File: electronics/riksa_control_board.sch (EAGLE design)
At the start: 13 parts, among them U1 ARDUINOR3-BPLACE

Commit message: ELE: new version of control board
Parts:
- removed BTN_REVERSE, BTN_STOP: (no value), adafruit:SWITCH_PUSHBUTTONSOFTTOUCHSMD_SJ
- removed LED_BACKWARD, LED_FORKWARD, LED_STOP: (no value), led:LED
- removed POT_LEFT, POT_RIGHT: (no value), rcl:POTENTIOMETER_PT-10S
- removed U1: ARDUINOR3-BPLACE, adafruit:ARDUINOR3-BPLACE
- added ARDUINO_NANO1: (no value), ArduinoNanoV30:ARDUINO_NANO
- added IM1: DEVKITC, esp32:DEVKITC
- added JP1: CON_ROBOCLAW, pinhead:PINHD-2X4
- added JP10, JP9: CON_MPU-6050, pinhead:PINHD-1X8
- added JP11: REPRO, pinhead:PINHD-2X2
- added JP12: VCC_REF_SEL, pinhead:PINHD-1X3
- added JP13: BLUETOOTH, pinhead:PINHD-1X5/90
- added JP2: POT_RIGHT, pinhead:PINHD-2X3
- added JP3: POT_LEFT, pinhead:PINHD-2X3
- added JP4: LED_STOP, pinhead:PINHD-2X2
- added JP5: LED_BACKWARD, pinhead:PINHD-2X2
- added JP6: LED_FORWARD, pinhead:PINHD-2X2
- added JP7: BTN_REVERSE, pinhead:PINHD-2X2
- added JP8: BTN_STOP, pinhead:PINHD-2X2
- added NC1, NC10, NC11, NC12, NC13, NC14, NC15, NC16, NC17, NC18, NC19, NC2, NC20, NC21, NC22, NC23, NC3, NC4, NC5, NC6, NC7, NC8, NC9: NC, NC:NC
- added R10, R9: x, rcl:R-EU_R0805
- added R6: 220, rcl:R-EU_R0805
- added R7: 2k2, rcl:R-EU_R0805
- added R8: 1k, rcl:R-EU_R0805
- R1, R2, R3, R4, R5: device rcl:R-EU_R0603 -> rcl:R-EU_R0805
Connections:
- removed net +5V: POT_LEFT.1, POT_RIGHT.1
- removed net ROBOCLAW_RX: U1.D0
- removed net ROBOCLAW_TX: U1.D1
- new net 3V3: ARDUINO_NANO1.3V3, IM1.3V3, JP12.1
- new net A0_POT_LEFT: ARDUINO_NANO1.ADC0/A0, IM1.IO26, JP3.3, JP3.4
- new net A1_POT_RIGHT: ARDUINO_NANO1.ADC1/A1, IM1.IO27, JP2.3, JP2.4
- new net AD0: JP10.7, JP9.7, NC1.NC
- new net BT_STATE: ARDUINO_NANO1.D7/AIN1, JP13.5
- new net D10_REPRO: ARDUINO_NANO1.D10/OC1B/!SS, IM1.IO25, R6.1
- new net D11_ROBOCLAW_RX: ARDUINO_NANO1.D11/MOSI, JP1.7, JP1.8
- new net D12_ROBOCLAW_TX: ARDUINO_NANO1.D12/MISO, JP1.5, JP1.6
- new net D3_BTN_STOP: ARDUINO_NANO1.D3/INT1, R1.1
- new net D4_BTN_REVERSE: ARDUINO_NANO1.D4/T0, R2.1
- new net D5_LED_FORWADR: ARDUINO_NANO1.D5/T1, R3.1
- new net D6_LED_BACKWARD: ARDUINO_NANO1.D6/AIN0, R4.1
- new net D9_LED_STOP: ARDUINO_NANO1.D9/OC1A, R5.1
- new net GND: ARDUINO_NANO1.GND@1, ARDUINO_NANO1.GND@2, IM1.GND, JP1.3, JP1.4, JP10.2, JP13.2, JP2.5, JP2.6, JP3.5, JP3.6, JP9.2, R10.2, R7.2
- new net MPU_INT: ARDUINO_NANO1.D2/INT0, JP10.8, JP9.8
- new net MPU_SCL: ARDUINO_NANO1.ADC5/SCL/A5, IM1.IO22, JP10.3, JP9.3
- new net MPU_SDA: ARDUINO_NANO1.ADC4/SDA/A4, IM1.IO21, JP10.4, JP9.4
- new net N$13: IM1.EN, NC11.NC
- new net N$15: IM1.IO12, NC17.NC
- new net N$16: IM1.IO15, NC18.NC
- new net N$17: IM1.IO2, NC19.NC
- new net N$18: IM1.IO0, NC20.NC
- new net N$19: IM1.IO5, NC21.NC
- new net N$20: ARDUINO_NANO1.SCK/D13, NC8.NC
- new net N$21: ARDUINO_NANO1.ADC3/A3, NC12.NC
- new net N$22: ARDUINO_NANO1.ADC6/A6, NC13.NC
- new net N$23: ARDUINO_NANO1.ADC7/A7, NC14.NC
- new net N$24: ARDUINO_NANO1.!RESET@1, NC15.NC
- new net N$25: ARDUINO_NANO1.D8/CLK0, NC16.NC
- new net N$26: ARDUINO_NANO1.!RESET@2, NC22.NC
- new net N$27: ARDUINO_NANO1.VIN, NC23.NC
- new net ROBOCLAW_GND1: JP11.3, JP11.4
- new net RX<-: ARDUINO_NANO1.D0/RX, IM1.RXD0, JP13.3
- new net TX->: ARDUINO_NANO1.D1/TX, IM1.TXD0, R8.2
- new net TX->_: JP13.4, R7.1, R8.1
- new net VCC: JP10.1, JP12.2, JP13.1, JP2.1, JP2.2, JP3.1, JP3.2, JP9.1
- new net VOLTAGE_REF: ARDUINO_NANO1.ADC2/A2, IM1.IO14, R10.1, R9.2
- new net XCL: JP10.6, JP9.6, NC2.NC
- new net XDA: JP10.5, JP9.5, NC3.NC
- net N$1: now also IM1.SD1, NC4.NC; no longer R3.1, U1.D5
- net N$10: now also IM1.SD3, NC9.NC; no longer BTN_STOP.P$1, R1.2
- net N$11: now also JP8.1, JP8.2, R1.2; no longer POT_LEFT.3, U1.A0
- net N$12: now also IM1.SD2, NC10.NC; no longer POT_RIGHT.3, U1.A1
- net N$2: now also JP11.1, JP11.2, R6.2; no longer R4.1, U1.D6
- net N$3: now also JP6.1, JP6.2; no longer LED_FORKWARD.A
- net N$4: now also JP5.1, JP5.2; no longer LED_BACKWARD.A
- net N$5: now also IM1.SD0, NC5.NC; no longer R5.1, U1.D11
- net N$6: now also IM1.CLK, NC6.NC; no longer R1.1, U1.D2
- net N$7: now also JP7.1, JP7.2, R2.2; no longer R2.1, U1.D3
- net N$8: now also JP4.1, JP4.2; no longer LED_STOP.A
- net N$9: now also IM1.CMD, NC7.NC; no longer BTN_REVERSE.P$1, R2.2
- net ROBOCLAW_5V: now also ARDUINO_NANO1.5V, IM1.5V, JP1.1, JP1.2, JP12.3, R9.1; no longer U1.5V
- net ROBOCLAW_GND: now also JP4.3, JP4.4, JP5.3, JP5.4, JP6.3, JP6.4, JP7.3, JP7.4, JP8.3, JP8.4; no longer BTN_REVERSE.P$2, BTN_STOP.P$2, LED_BACKWARD.C, LED_FORKWARD.C, LED_STOP.C, POT_LEFT.2, POT_RIGHT.2, U1.GND1
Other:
- note added: "Info: Arduino Nano: add R7 + R8 (for 5V device) ESP32: R8 = 0 Ohm and without R7"
- moved on the sheet: R1, R2, R3, R4, R5

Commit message: ELE: final version of control board
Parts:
- added JP14: EMPTY, pinhead:PINHD-1X2
- added NC24: NC, NC:NC
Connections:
- net N$11 renamed D3_BTN_STOP_
- net N$2 renamed D10_REPRO_
- net N$3 renamed D5_LED_FORWADR_
- net N$4 renamed D6_LED_BACKWARD_
- net N$7 renamed D4_BTN_REVERSE_
- net N$8 renamed D9_LED_STOP_
- removed net ROBOCLAW_GND: JP4.3, JP4.4, JP5.3, JP5.4, JP6.3, JP6.4, JP7.3, JP7.4, JP8.3, JP8.4
- removed net ROBOCLAW_GND1: JP11.3, JP11.4
- new net IO18: IM1.IO18, JP14.2
- new net IO19: IM1.IO19, JP14.1
- new net N$14: ARDUINO_NANO1.AREF, NC24.NC
- net BT_STATE: now also IM1.SVP
- net D11_ROBOCLAW_RX: now also IM1.IO33
- net D12_ROBOCLAW_TX: now also IM1.IO32
- net D3_BTN_STOP: now also IM1.IO35
- net D4_BTN_REVERSE: now also IM1.IO34
- net D5_LED_FORWADR: now also IM1.IO16
- net D6_LED_BACKWARD: now also IM1.IO17
- net D9_LED_STOP: now also IM1.IO4
- net GND: now also JP11.3, JP11.4, JP4.3, JP4.4, JP5.3, JP5.4, JP6.3, JP6.4, JP7.3, JP7.4, JP8.3, JP8.4
- net MPU_INT: now also IM1.SVN

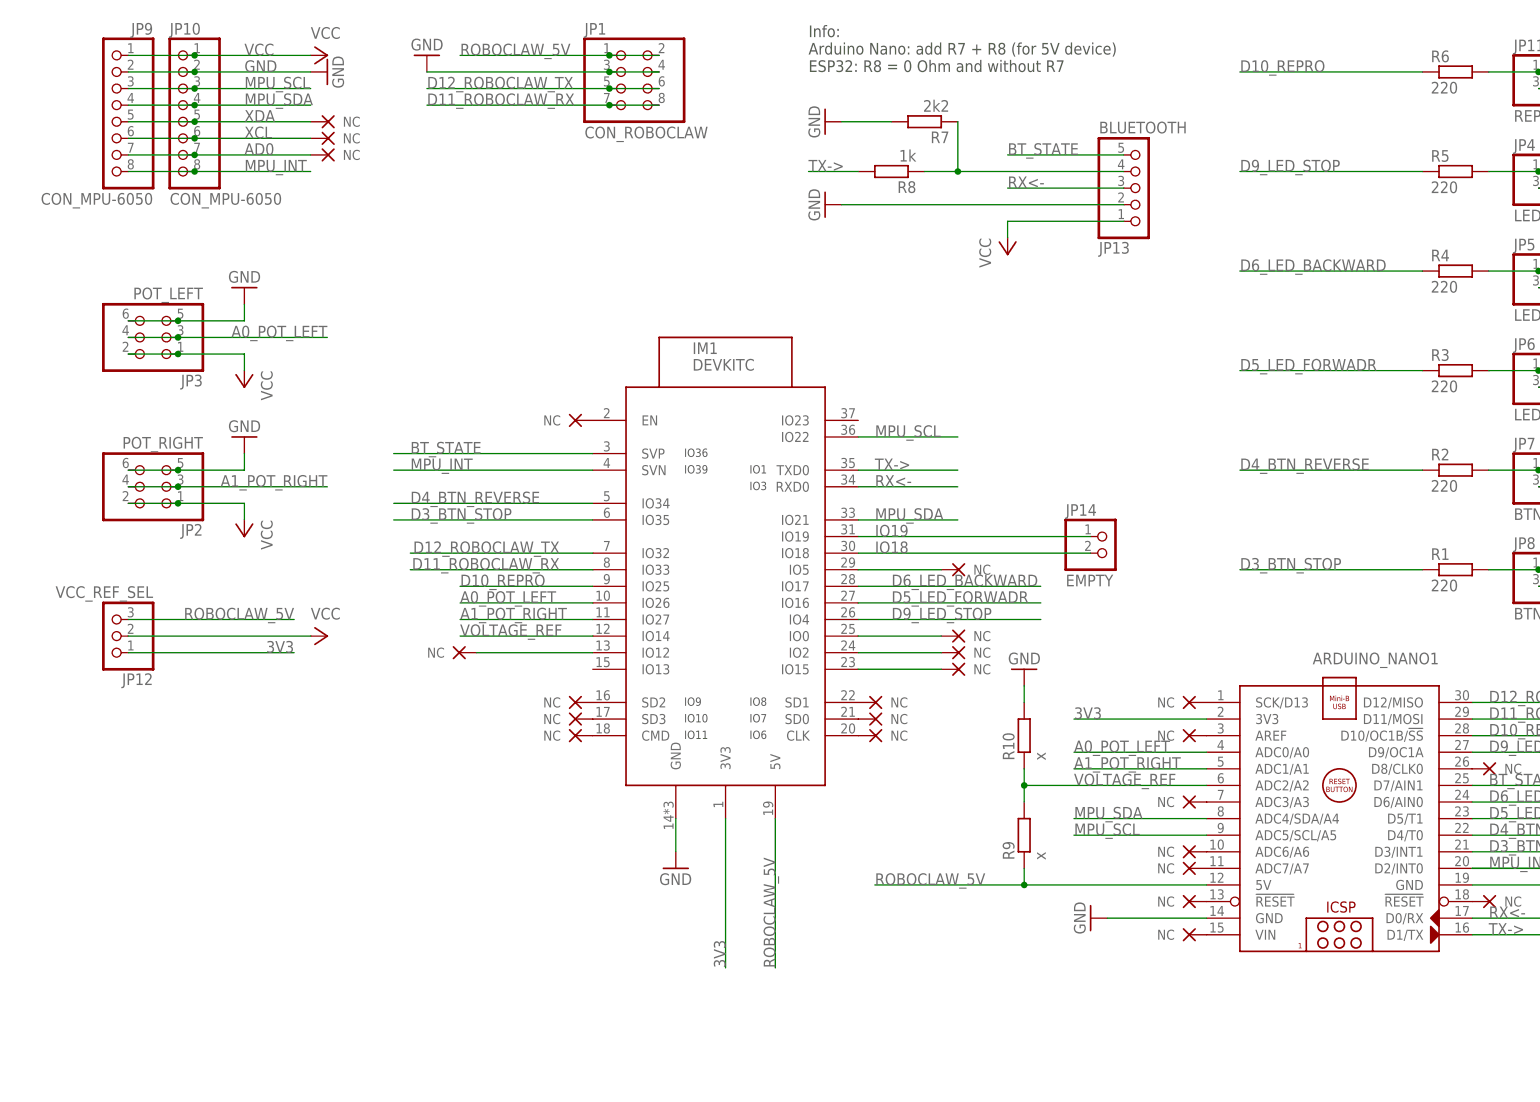
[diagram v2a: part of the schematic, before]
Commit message: ELE: fix Kubas comments
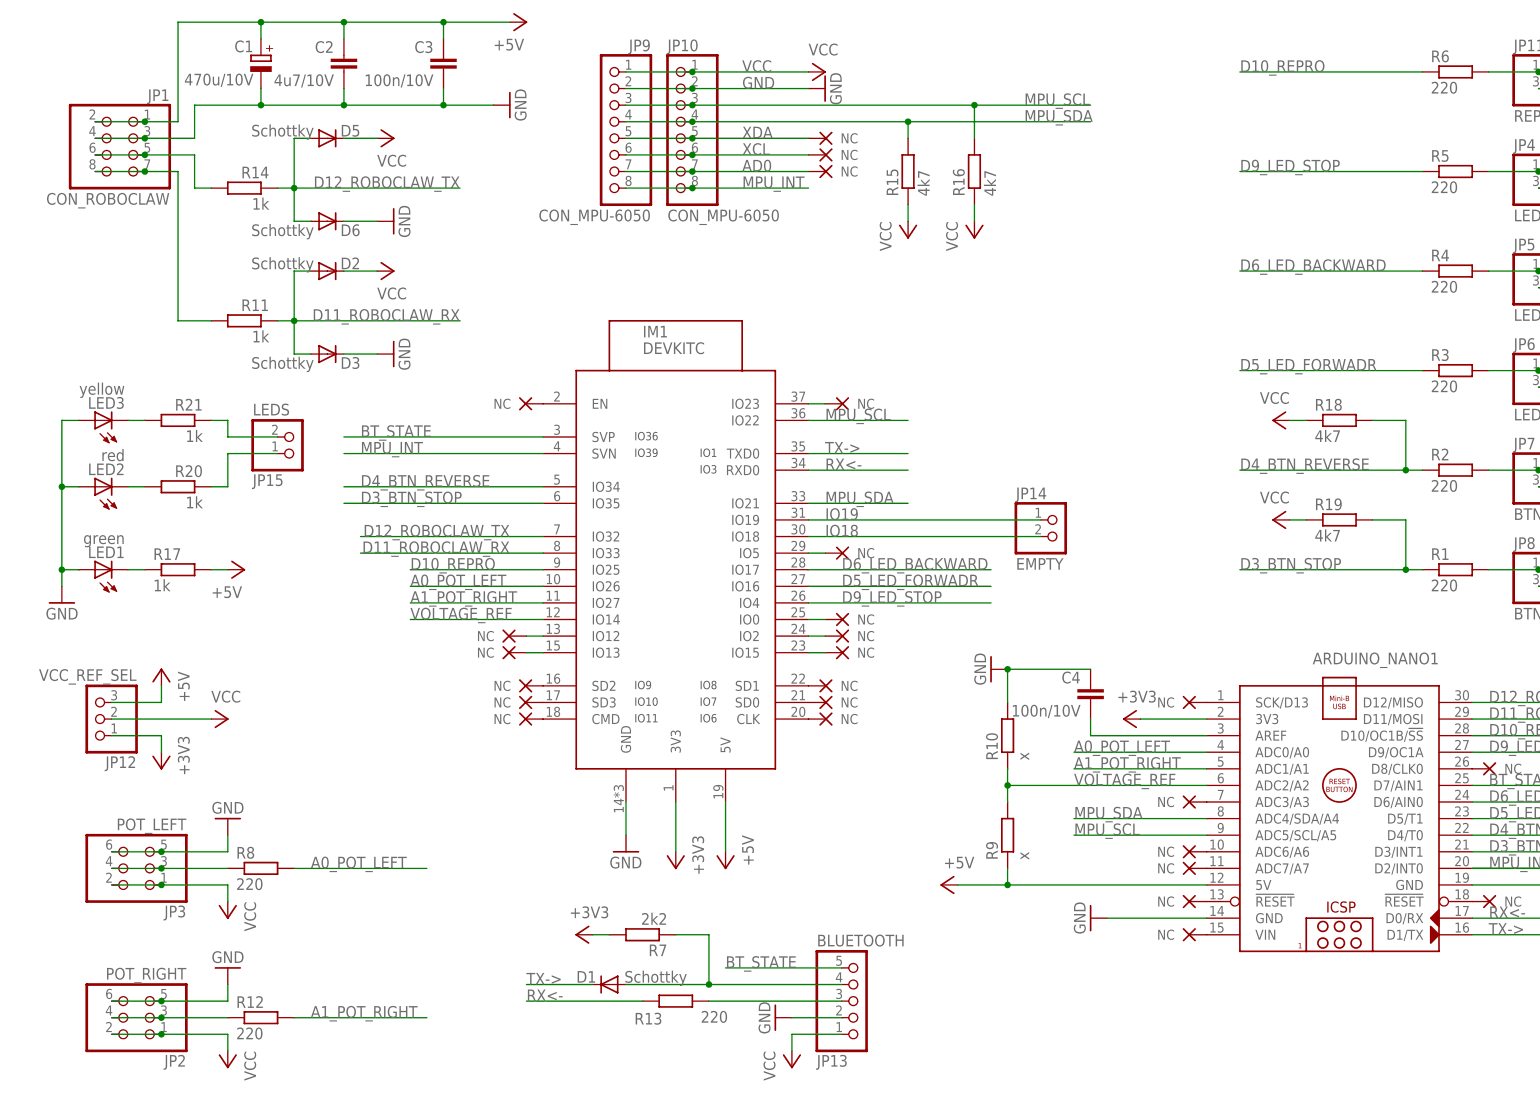
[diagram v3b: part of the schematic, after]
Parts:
- removed NC24: NC, NC:NC
- added C1: 470u/10V, rcl:CPOL-EUTT6D6
- added C2: 4u7/10V, rcl:C-EUC0805
- added C3, C4: 100n/10V, rcl:C-EUC0603
- added D1, D2, D3, D5, D6: Schottky, diode:DIODE-0603
- added JP15: LEDS, pinhead:PINHD-1X2
- added LED1: green, led:LEDCHIPLED_0603
- added LED2: red, led:LEDCHIPLED_0603
- added LED3: yellow, led:LEDCHIPLED_0603
- added NC25, NC27: NC, NC:NC
- added R11, R14, R17, R20, R21: 1k, rcl:R-EU_R0805
- added R12, R13: 220, rcl:R-EU_R0805
- added R15, R16, R18, R19: 4k7, rcl:R-EU_R0805
- R8: value 1k -> 220
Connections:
- removed net 3V3: ARDUINO_NANO1.3V3, IM1.3V3, JP12.1
- removed net N$14: ARDUINO_NANO1.AREF, NC24.NC
- removed net ROBOCLAW_5V: ARDUINO_NANO1.5V, IM1.5V, JP1.1, JP1.2, JP12.3, R9.1
- new net +3V3: ARDUINO_NANO1.3V3, IM1.3V3, JP12.1, R7.2
- new net +5V: ARDUINO_NANO1.5V, C1.+, C2.1, C3.1, IM1.5V, JP1.1, JP1.2, JP12.3, R17.2, R9.1
- new net A0_POT_LEFT_: JP3.3, JP3.4, R8.1
- new net A1_POT_RIGHT_: JP2.3, JP2.4, R12.1
- new net D11_ROBOCLAW_RX_: JP1.7, JP1.8, R11.2
- new net D12_ROBOCLAW_TX_: JP1.5, JP1.6, R14.2
- new net LED_GREEN_: LED1.C, R17.1
- new net LED_RED: JP15.1, R20.1
- new net LED_RED_: LED2.C, R20.2
- new net LED_YELLOW: JP15.2, R21.1
- new net LED_YELLOW_: LED3.C, R21.2
- new net N$3: IM1.IO23, NC25.NC
- new net N$4: IM1.IO13, NC27.NC
- new net N$7: ARDUINO_NANO1.AREF, C4.2
- new net RX<-_: JP13.3, R13.2
- net A0_POT_LEFT: now also R8.2; no longer JP3.3, JP3.4
- net A1_POT_RIGHT: now also R12.2; no longer JP2.3, JP2.4
- net D11_ROBOCLAW_RX: now also D2.A, D3.A, R11.1; no longer JP1.7, JP1.8
- net D12_ROBOCLAW_TX: now also D5.A, D6.A, R14.1; no longer JP1.5, JP1.6
- net D3_BTN_STOP: now also R19.2
- net D4_BTN_REVERSE: now also R18.2
- net GND: now also C1.-, C2.2, C3.2, C4.1, D3.C, D6.C, LED1.A, LED2.A, LED3.A; no longer R7.2
- net MPU_SCL: now also R16.2
- net MPU_SDA: now also R15.2
- net RX<-: now also R13.1; no longer JP13.3
- net TX->: now also D1.C; no longer R8.2
- net TX->_: now also D1.A; no longer R8.1
- net VCC: now also D2.C, D5.C, R15.1, R16.1, R18.1, R19.1
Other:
- note removed: "Info: Arduino Nano: add R7 + R8 (for 5V device) ESP32: R8 = 0 Ohm and without R7"
- moved on the sheet: IM1, JP1, JP10, JP12, JP13, JP14, JP2, JP3, JP9, R10, R7, R8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
